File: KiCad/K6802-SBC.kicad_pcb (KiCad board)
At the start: 2 copper layers, 100 x 75 mm, 47 parts, among them J1 Barrel_Jack_Switch, J2 SBC6303 BUS, J3 SERIAL JP, SW1 POWER, SW2 RESET, U1 74LS00, U2 74LS00, U3 MC6802, U4 74LS138, U5 HM628128D_DIP32_SOP32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

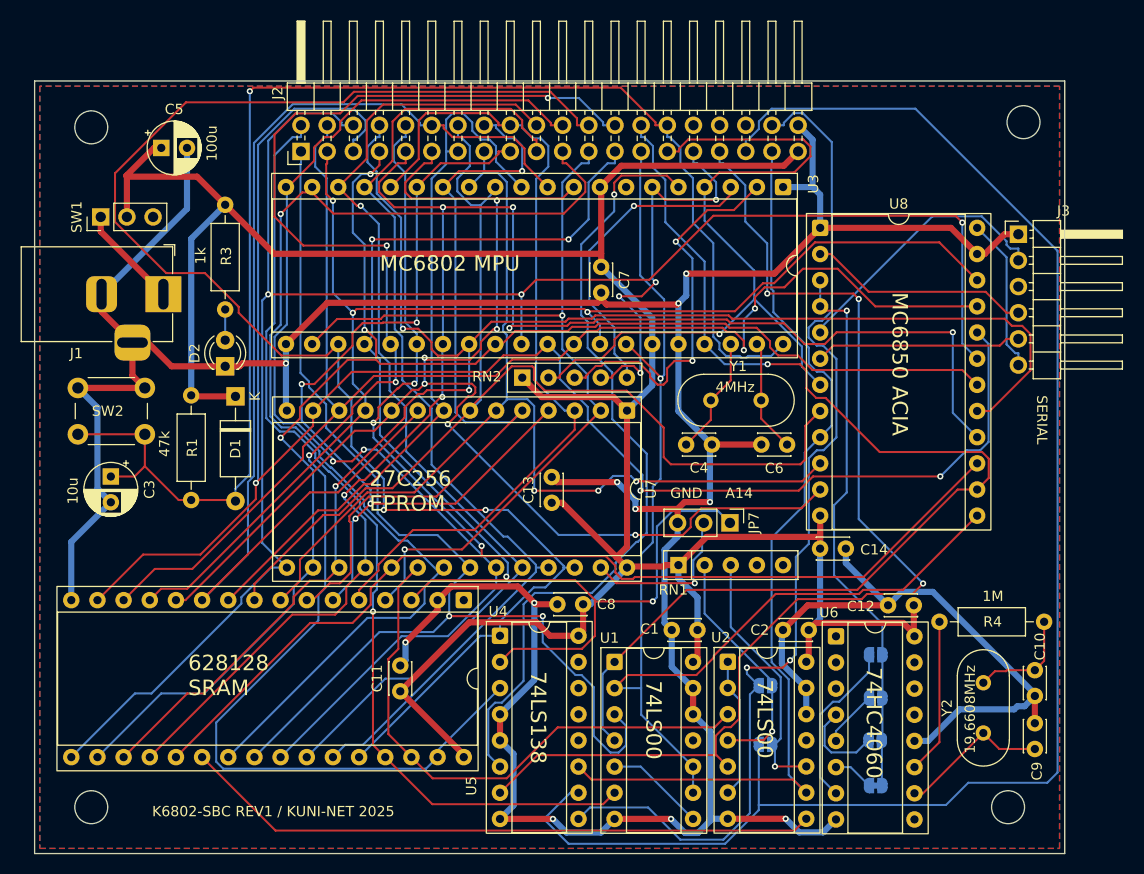
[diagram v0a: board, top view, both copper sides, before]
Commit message: $C000無効かジャンパ追加 REV2ガーバー出力
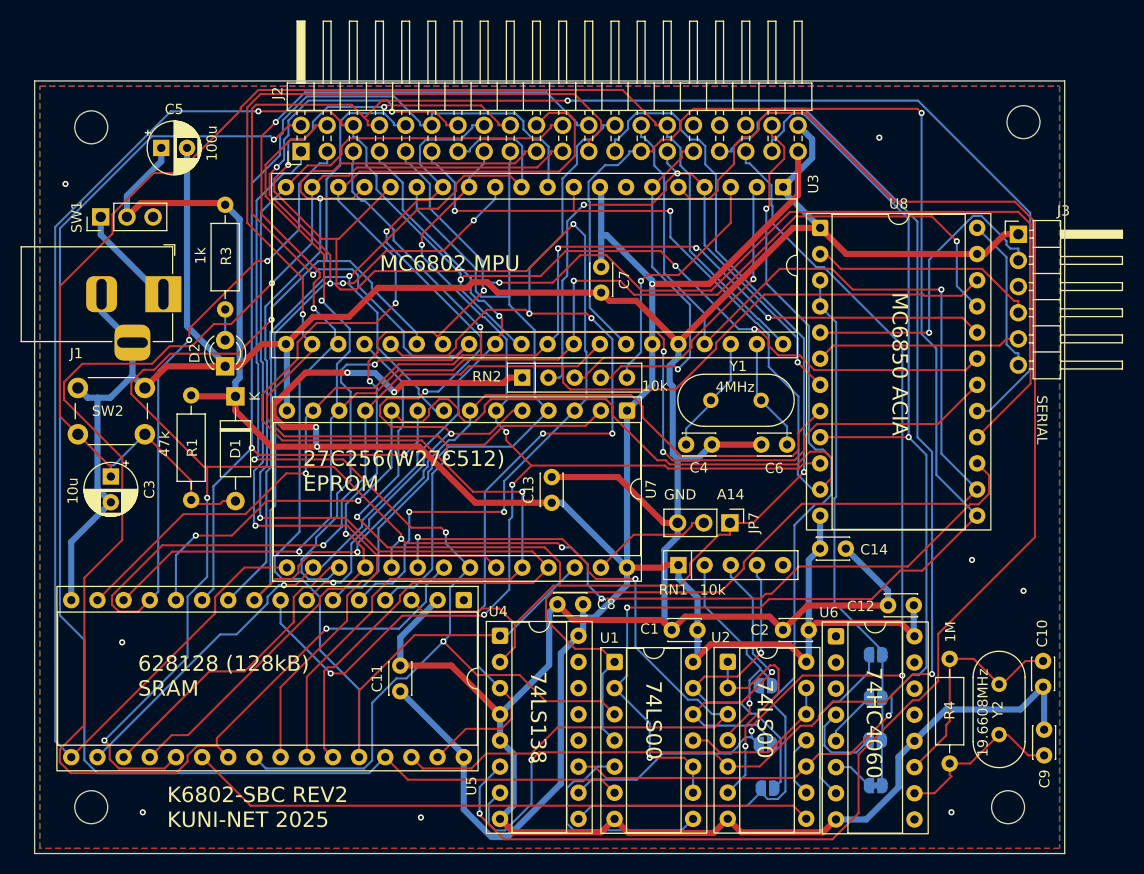
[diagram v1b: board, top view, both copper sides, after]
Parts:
- added JP8: C000_JP, Jumper:SolderJumper-2_P1.3mm_Open_RoundedPad1.0x1.5mm, B.Cu at (161.2, 118.7)
- JP1: value C000_JP -> 16k_JP
- moved R4 13.8 mm to (178.8, 116.3), turned to 90 degrees
- moved Y2 1.54 mm to (183.6, 113.5)
- moved C10 1.20 mm to (187.9, 108.8)
- moved C9 1.09 mm to (188.0, 113.0)
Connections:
- net /~{RAM_DIABLE} renamed /RAM_DIABLE
- C10 pad 2: Net-(C10-Pad2) -> Net-(U6-~{Φ1})
- R4 pad 1: Net-(U6-~{Φ1}) -> Net-(U6-Φ0)
- R4 pad 2: Net-(C10-Pad2) -> Net-(U6-~{Φ1})
- RN1 pad 4: unconnected-(RN1-R3-Pad4) -> Net-(JP8-B)
- U1 pad 11: unconnected-(U1-Pad11) -> Net-(U1-Pad11)
- U1 pad 12: GND -> Net-(JP2-B)
- U1 pad 13: GND -> Net-(JP8-B)
- U2 pad 10: Net-(JP2-B) -> /$8000
- U2 pad 11: unconnected-(U2-Pad11) -> Net-(U2-Pad11)
- U2 pad 12: GND -> Net-(U1-Pad11)
- U2 pad 13: GND -> Net-(U1-Pad11)
- U2 pad 9: /$8000 -> Net-(U2-Pad11)
- Y2 pad 2: Net-(C10-Pad2) -> Net-(U6-~{Φ1})
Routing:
- net /VMA: track 78.2 -> 154.2 mm
- net /D7: track 142.9 -> 203.8 mm, vias 3 -> 6
- net /D5: track 155.8 -> 214.7 mm
- net /$A000: track 153.5 -> 95.6 mm, vias 0 -> 2
- net /A3: track 108.8 -> 163.9 mm, vias 0 -> 6
- net /A7: track 80.9 -> 127.9 mm, vias 0 -> 5
- net /A12: track 84.0 -> 127.5 mm
- net /A15: track 147.5 -> 104.5 mm
- net /D0: track 124.1 -> 166.6 mm
- net /A10: track 110.6 -> 152.0 mm, vias 1 -> 2
- net /~{WR}: track 93.8 -> 134.5 mm
- net /R/~{W}: track 115.9 -> 156.1 mm, vias 1 -> 3
- net /A9: track 98.8 -> 135.3 mm, vias 1 -> 2
- net VCC: track 261.1 -> 297.0 mm, vias 0 -> 5
- net /D2: track 169.6 -> 136.3 mm, vias 3 -> 5
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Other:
- board text added: "$A000"
- board text added: "$C000"
- board text added: "10k"
- board text added: "27C256(W27C512) EPROM"
- board text added: "628128 (128kB) SRAM"
- board text added: "K6802-SBC REV2 KUNI-NET 2025"
- board text added: "ROM16k"
- board text removed: "27C256 EPROM"
- board text removed: "628128 SRAM"
- board text removed: "K6802-SBC REV1 / KUNI-NET 2025"
